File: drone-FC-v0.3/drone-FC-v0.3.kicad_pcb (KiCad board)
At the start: 2 copper layers, 68 parts, among them J1 USB_C_Receptacle_USB2.0_16P, J10 M1, J11 USB_C_Receptacle_USB2.0_16P, J2 Conn_01x04_Pin, J3 S2, J4 S3, J5 S1, J6 Conn_01x04_Pin, J7 ICM, J8 UART0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

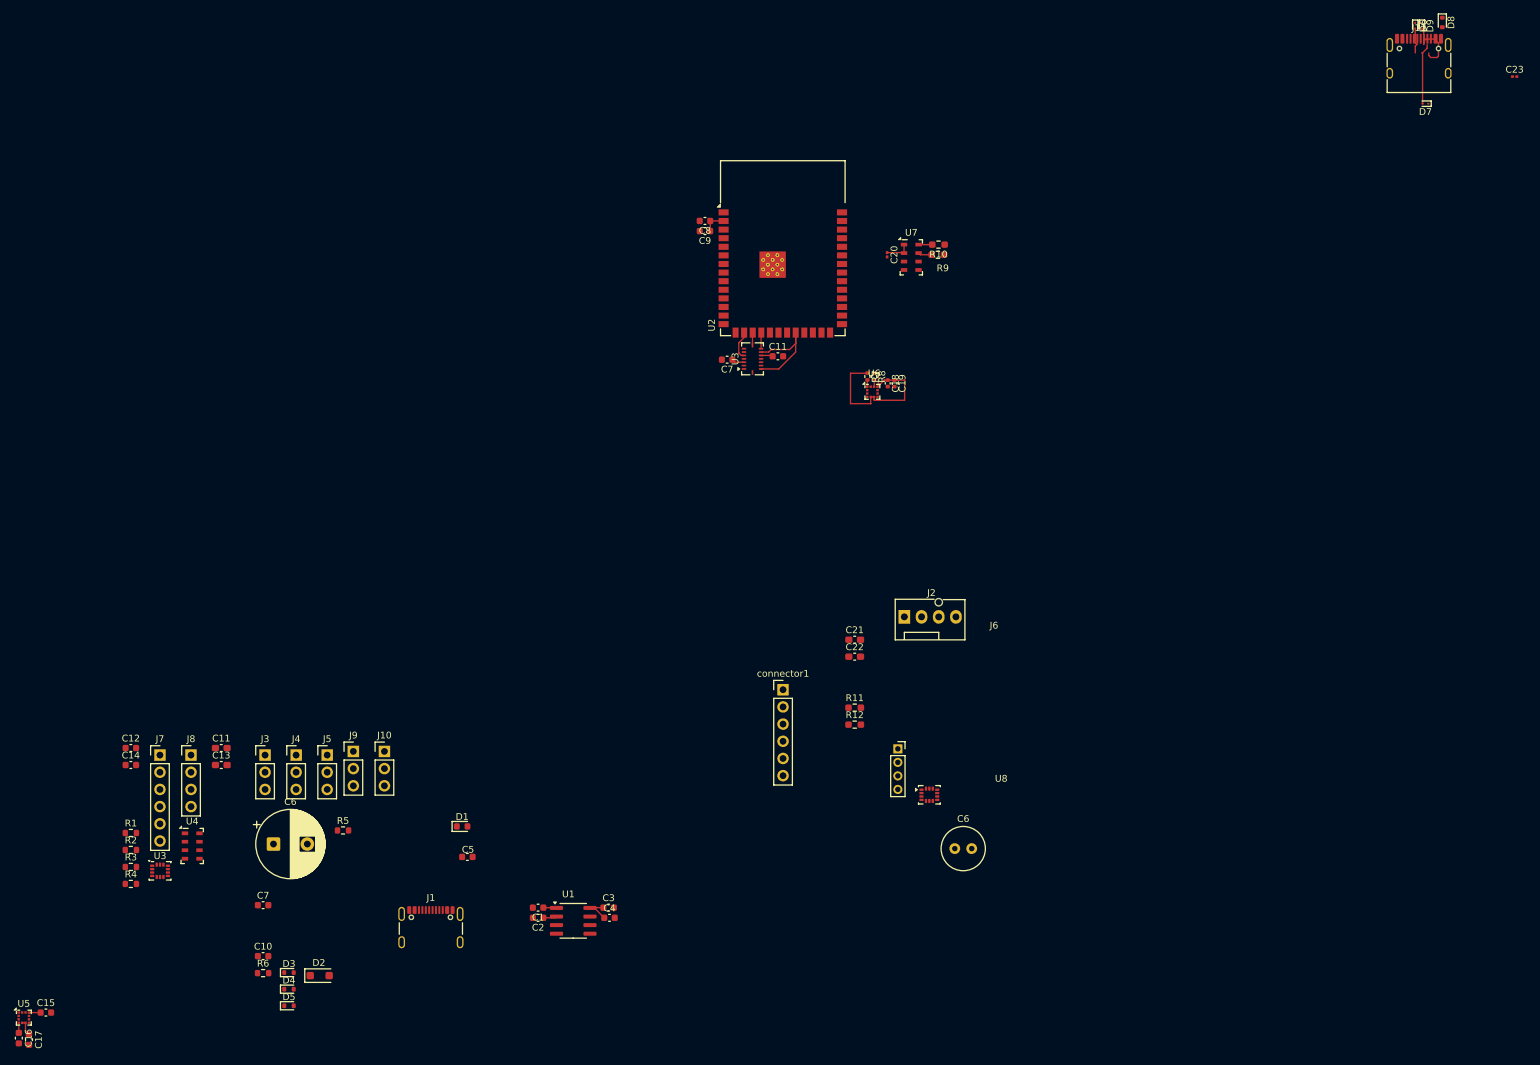
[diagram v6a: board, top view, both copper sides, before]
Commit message: added connections and ground plane
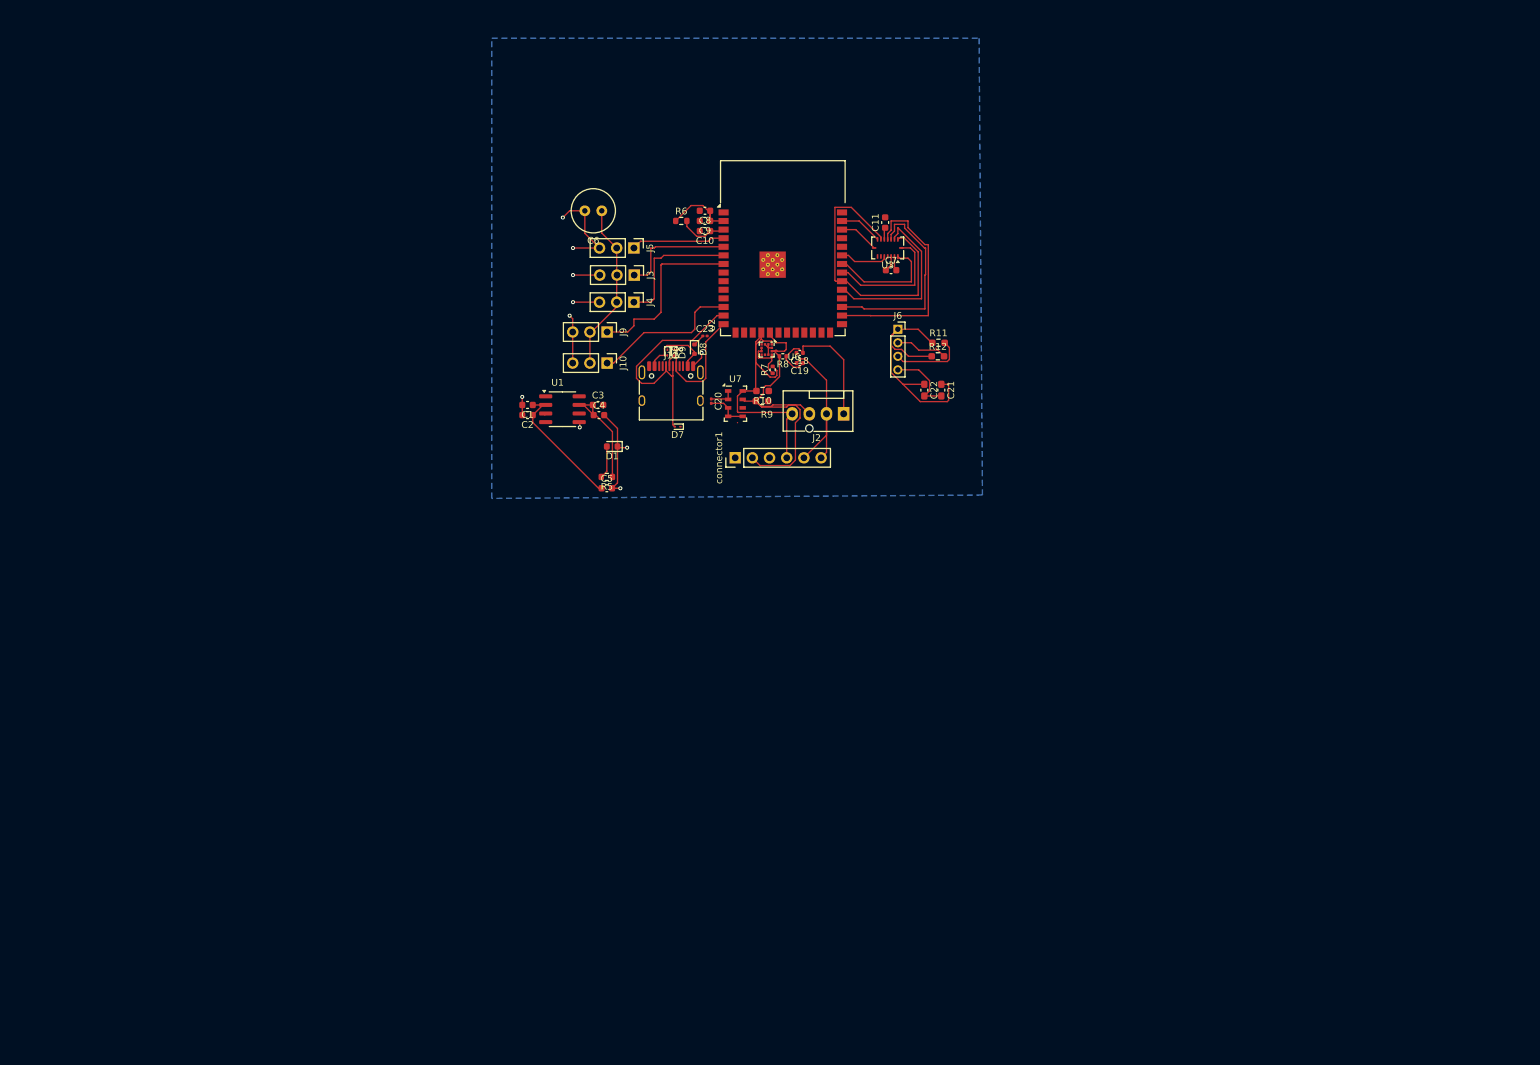
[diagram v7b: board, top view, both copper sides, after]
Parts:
- removed the C11 at (55.0, 129.9)
- removed C12: 4.7uF, Capacitor_SMD:C_0603_1608Metric
- removed C13: 0.1uF, Capacitor_SMD:C_0603_1608Metric_Pad1.08x0.95mm_HandSolder
- removed C14, C16, C17: 0.1uF, Capacitor_SMD:C_0603_1608Metric
- removed C15: 1uF, Capacitor_SMD:C_0603_1608Metric
- removed the C6 at (62.7, 144.1)
- removed the C7 at (61.2, 153.1)
- removed D2: D, Diode_SMD:D_SOD-123F
- removed D3, D4, D5: D, Diode_SMD:D_SOD-523
- removed J1: USB_C_Receptacle_USB2.0_16P, Connector_USB:USB_C_Receptacle_GCT_USB4105-xx-A_16P_TopMnt_Horizontal
- removed J7: ICM, Connector_PinHeader_2.54mm:PinHeader_1x06_P2.54mm_Vertical
- removed J8: UART0, Connector_PinHeader_2.54mm:PinHeader_1x04_P2.54mm_Vertical
- removed R1, R2, R3, R4: 4.7k, Resistor_SMD:R_0603_1608Metric
- removed the U3 at (46.0, 148.0)
- removed U4: MS5607-02BA, Package_LGA:LGA-8_3x5mm_P1.25mm
- removed U5: LIS3MDL, Package_LGA:LGA-12_2x2mm_P0.5mm
- removed U8: LSM6DSOX, Package_LGA:LGA-14_3x2.5mm_P0.5mm_LayoutBorder3x4y
- moved R6 127.2 mm to (123.0, 52.0)
- moved C23 125.6 mm to (126.5, 69.0)
- moved C10 125.5 mm to (126.5, 53.5), turned to 180 degrees
- moved J11 120.6 mm to (121.5, 77.5)
- moved D6 120.6 mm to (121.0, 71.5)
- moved D8 120.6 mm to (125.0, 71.0)
- moved D9 120.6 mm to (122.0, 71.5)
- moved D7 120.4 mm to (122.5, 82.4)
- moved C6 107.7 mm to (111.2, 50.5), turned to 180 degrees
- moved J3 89.5 mm to (116.0, 60.0), turned to -90 degrees
- moved J5 87.6 mm to (116.0, 56.0), turned to -90 degrees
- moved J4 83.5 mm to (116.0, 64.0), turned to -90 degrees
- moved U1 75.6 mm to (105.4, 79.8)
- moved C1 74.3 mm to (100.3, 79.2)
- moved C2 74.3 mm to (100.3, 80.7)
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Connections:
- J2 pad 3: SDA_MAG -> SDA
- J2 pad 4: SCL_MAG -> SCL
- U2 pad 15: SCLK -> unconnected-(U2-IO3-Pad15)
- U2 pad 16: MOSI -> unconnected-(U2-IO46-Pad16)
- U2 pad 17: CSB_GYRO -> unconnected-(U2-IO9-Pad17)
- U2 pad 28: unconnected-(U2-IO35-Pad28) -> GPIO28
- U2 pad 29: unconnected-(U2-IO36-Pad29) -> GPIO29
- U2 pad 31: unconnected-(U2-IO38-Pad31) -> GPIO38
- U2 pad 32: unconnected-(U2-IO39-Pad32) -> MISO
- U2 pad 33: unconnected-(U2-IO40-Pad33) -> GPIO40
- U2 pad 34: unconnected-(U2-IO41-Pad34) -> GPIO41
- U2 pad 35: MISO -> CSB_GYRO
- U2 pad 38: unconnected-(U2-IO2-Pad38) -> SCLK
- U2 pad 39: unconnected-(U2-IO1-Pad39) -> MOSI
- U3 pad 1: GPIO5 -> GPIO41
- U3 pad 12: GPIO6 -> GPIO28
- U3 pad 13: GPIO7 -> GPIO29
- U3 pad 14: GPIO15 -> GPIO38
- U3 pad 16: GPIO4 -> GPIO40
- connector1 pad 2: SDO1 -> SDA
- connector1 pad 4: SCLK -> SCL
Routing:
- net GND: track 0.00 -> 98.2 mm, vias 0 -> 11
- net SDA: track 3.02 -> 50.3 mm
- net +5V: track 3.98 -> 46.6 mm
- net +3.3V: track 1.76 -> 41.1 mm
- net SCL: track 3.04 -> 42.2 mm
- net GPIO28: track 0.00 -> 34.0 mm
- net GPIO29: track 0.00 -> 30.2 mm
- net MISO: track 16.3 -> 43.3 mm
- net GPIO38: track 0.00 -> 26.2 mm
- net GPIO 7: track 0.00 -> 26.1 mm
- net USB_D-: track 9.13 -> 35.2 mm
- net GPIO 8: track 0.00 -> 22.1 mm
- net GPIO 6: track 0.00 -> 19.6 mm
- net GPIO40: track 0.00 -> 19.2 mm
- net +3V3: track 38.8 -> 58.0 mm
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- added copper zone on B.Cu, net GND
